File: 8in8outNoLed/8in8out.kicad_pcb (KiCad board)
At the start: 2 copper layers, 90 parts, among them IC1 ATTINY2313-P, J1 RJ45, J2 RJ45, J3 CONN_6, K110 G5T-1-12VDC, K120 G5T-1-12VDC, K130 G5T-1-12VDC, K140 G5T-1-12VDC, K150 G5T-1-12VDC, K160 G5T-1-12VDC, K170 G5T-1-12VDC, K180 G5T-1-12VDC, P1 CONN_5, P100 CONN_2, P101 CONN_2, P102 CONN_2, P103 CONN_2, P105 CONN_2, P106 CONN_2, P107 CONN_8, P109 CONN_2, P110 CONN_2, P120 CONN_2, P130 CONN_2, P140 CONN_2, P150 CONN_2, P160 CONN_2, P170 CONN_2, P180 CONN_2, P2 CONN_5, Q110 NPN, Q120 NPN, Q130 NPN, Q140 NPN, Q150 NPN, Q160 NPN, Q170 NPN, Q180 NPN, U1 74HC595, U10 OPTO-TRANSISTOR, U2 74LS165, U20 OPTO-TRANSISTOR, U30 OPTO-TRANSISTOR, U40 OPTO-TRANSISTOR, U50 OPTO-TRANSISTOR, U60 OPTO-TRANSISTOR, U70 OPTO-TRANSISTOR, U80 OPTO-TRANSISTOR

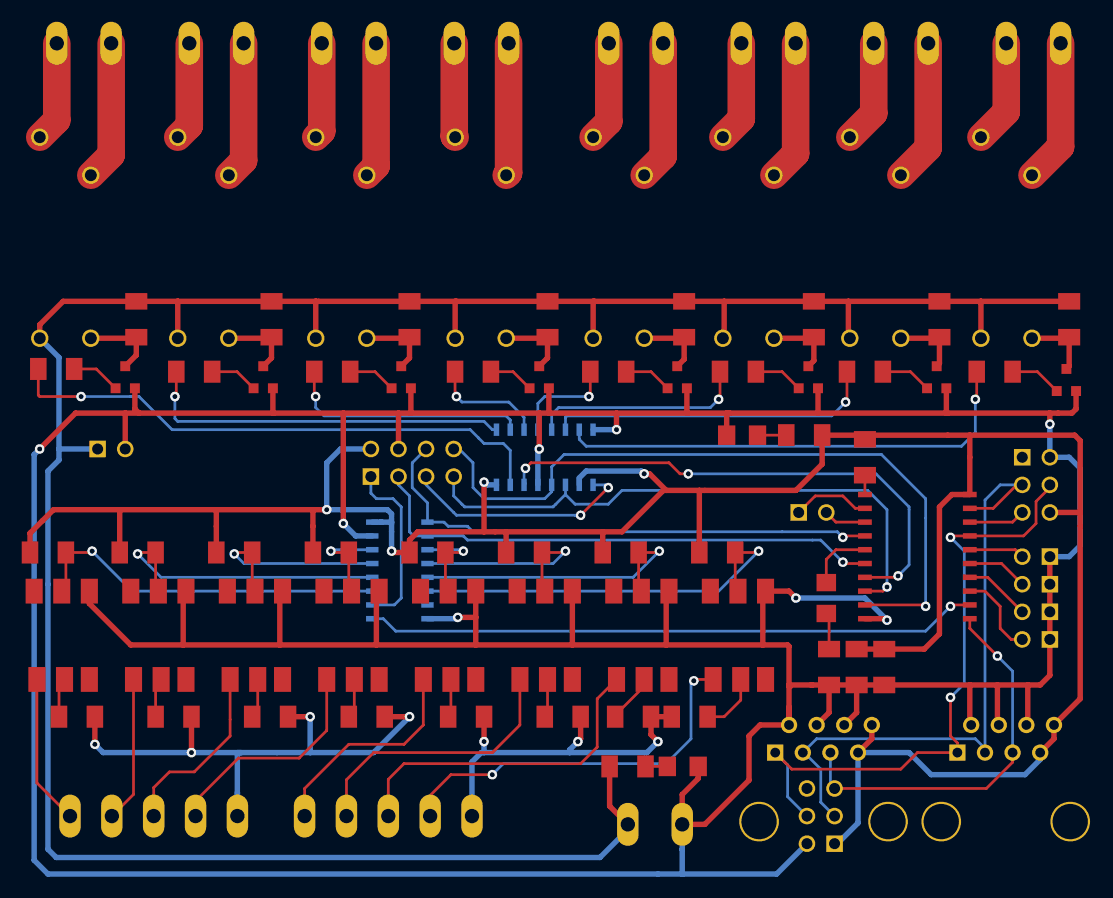
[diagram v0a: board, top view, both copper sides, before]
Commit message: ajout deux points par relais pour bypasser le NPN et commander le relais en direct (mode secours update .brd
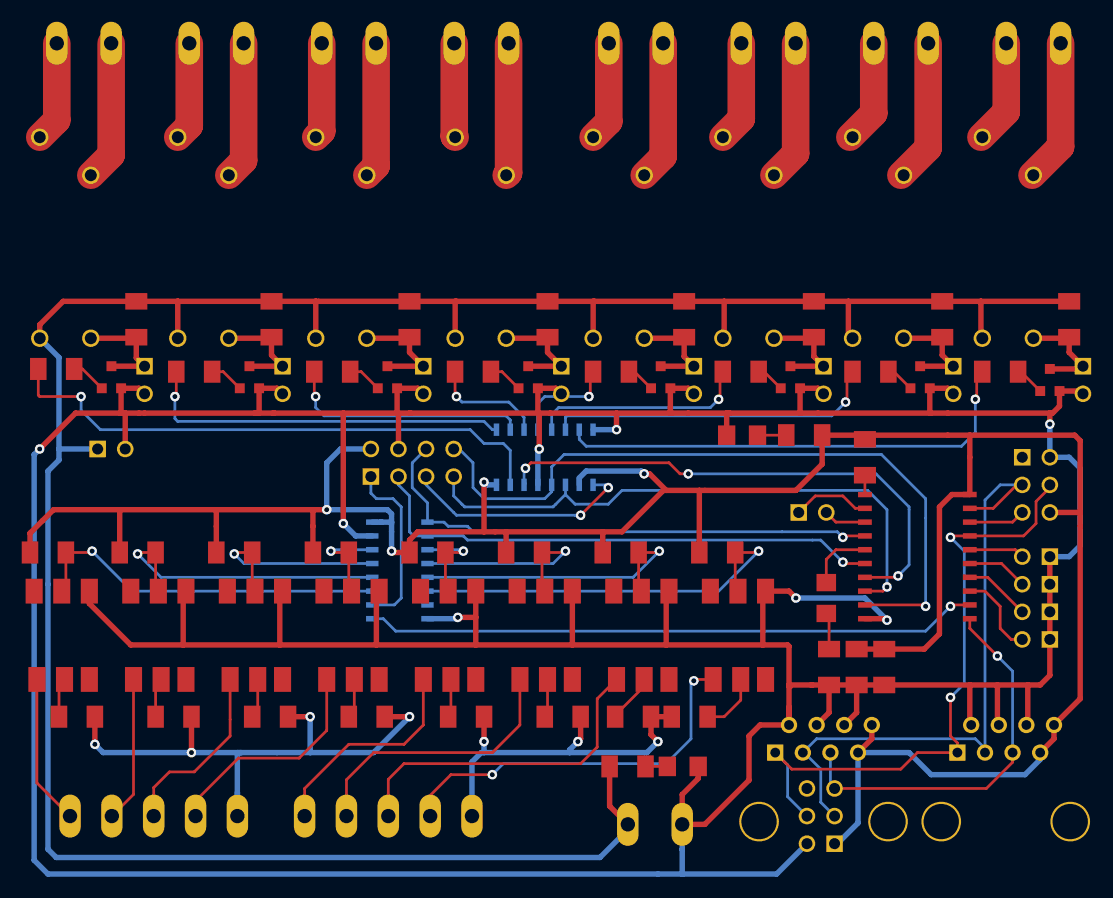
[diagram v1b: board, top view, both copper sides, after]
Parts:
- added P111: CONN_2, PIN_ARRAY_2X1, F.Cu at (193.5, 109.7)
- added P121: CONN_2, PIN_ARRAY_2X1, F.Cu at (206.2, 109.7)
- added P131: CONN_2, PIN_ARRAY_2X1, F.Cu at (219.2, 109.7)
- added P141: CONN_2, PIN_ARRAY_2X1, F.Cu at (231.9, 109.7)
- added P151: CONN_2, PIN_ARRAY_2X1, F.Cu at (244.1, 109.7)
- added P161: CONN_2, PIN_ARRAY_2X1, F.Cu at (256.0, 109.7)
- added P171: CONN_2, PIN_ARRAY_2X1, F.Cu at (268.0, 109.7)
- added P181: CONN_2, PIN_ARRAY_2X1, F.Cu at (279.9, 109.7)
- moved Q160 1.65 mm to (253.0, 109.5)
- moved Q150 1.52 mm to (241.0, 109.5)
- moved Q170 1.52 mm to (264.9, 109.5)
- moved Q180 1.52 mm to (276.9, 109.7)
- moved Q110 1.27 mm to (190.5, 109.5)
- moved Q120 1.27 mm to (203.2, 109.5)
- moved Q130 1.27 mm to (215.9, 109.5)
- moved Q140 1.02 mm to (228.9, 109.5)
- moved R171 0.51 mm to (260.4, 109.0)
- moved R181 0.51 mm to (272.3, 109.0)
- moved D171 0.25 mm to (267.0, 104.1)
- moved R161 0.25 mm to (248.4, 109.0)
- moved R151 0.25 mm to (236.5, 109.0)
- moved K170 0.25 mm to (257.6, 106.9)
- moved K180 0.13 mm to (269.5, 106.9)
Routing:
- net DGND: track 490.1 -> 508.0 mm
- net /C130: track 6.95 -> 10.5 mm
- net /C170: track 6.36 -> 9.72 mm
- net /C180: track 6.49 -> 9.81 mm
- net /C140: track 6.82 -> 10.1 mm
- net /C160: track 6.59 -> 9.80 mm
- net /C120: track 6.95 -> 10.1 mm
- net /C150: track 6.64 -> 9.80 mm
- net /C110: track 7.31 -> 10.3 mm
- net N-0000034: track 4.80 -> 2.77 mm
- net N-0000033: track 4.70 -> 2.66 mm
- net N-0000040: track 4.57 -> 2.66 mm
- net N-0000039: track 4.44 -> 2.66 mm
- net N-0000050: track 4.44 -> 3.17 mm
- net N-0000051: track 4.55 -> 3.28 mm
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
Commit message: Mis au propre du sch?ma
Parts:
- U2: value 74LS165 -> 74HC165
- moved P107 0.51 mm to (218.2, 117.9)
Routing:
- net OUT4: track 9.71 -> 20.0 mm
- net DGND: track 508.0 -> 508.6 mm
- net CLK_IN: track 48.6 -> 48.1 mm
- net +5V: track 250.7 -> 250.2 mm
- net U2_IN: track 16.2 -> 15.6 mm
- net LATCH_IN: track 48.7 -> 48.2 mm

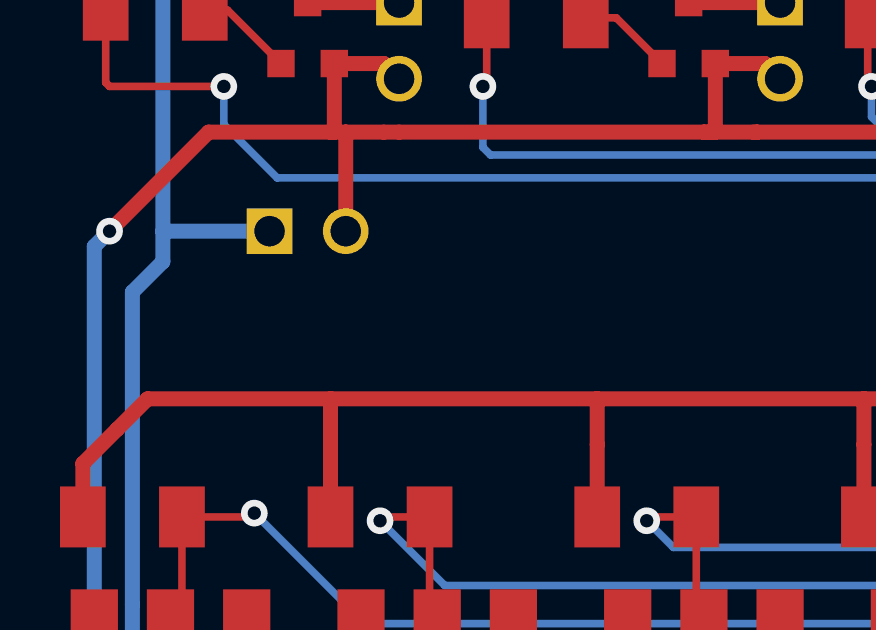
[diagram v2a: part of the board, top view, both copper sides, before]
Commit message: ajout d'un connecteur 12v-Gnd-5v (P200)
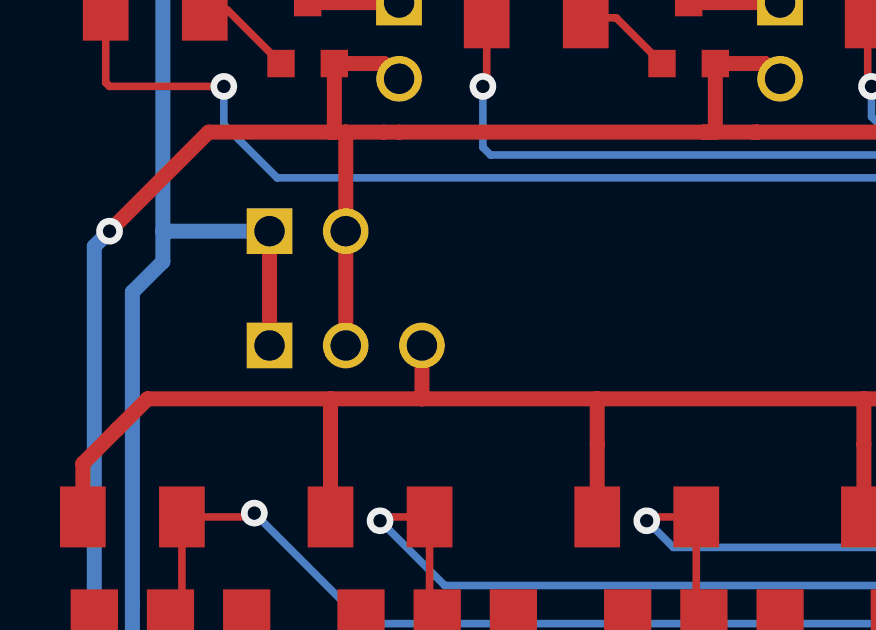
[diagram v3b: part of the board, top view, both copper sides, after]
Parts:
- added P200: CONN_3, PIN_ARRAY_3X1, F.Cu at (191.8, 119.9)
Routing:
- net +12V: track 234.9 -> 238.7 mm
- net DGND: track 508.6 -> 512.5 mm
- net +5V: track 250.2 -> 252.0 mm
